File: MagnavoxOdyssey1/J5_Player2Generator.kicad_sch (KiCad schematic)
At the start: 19 parts

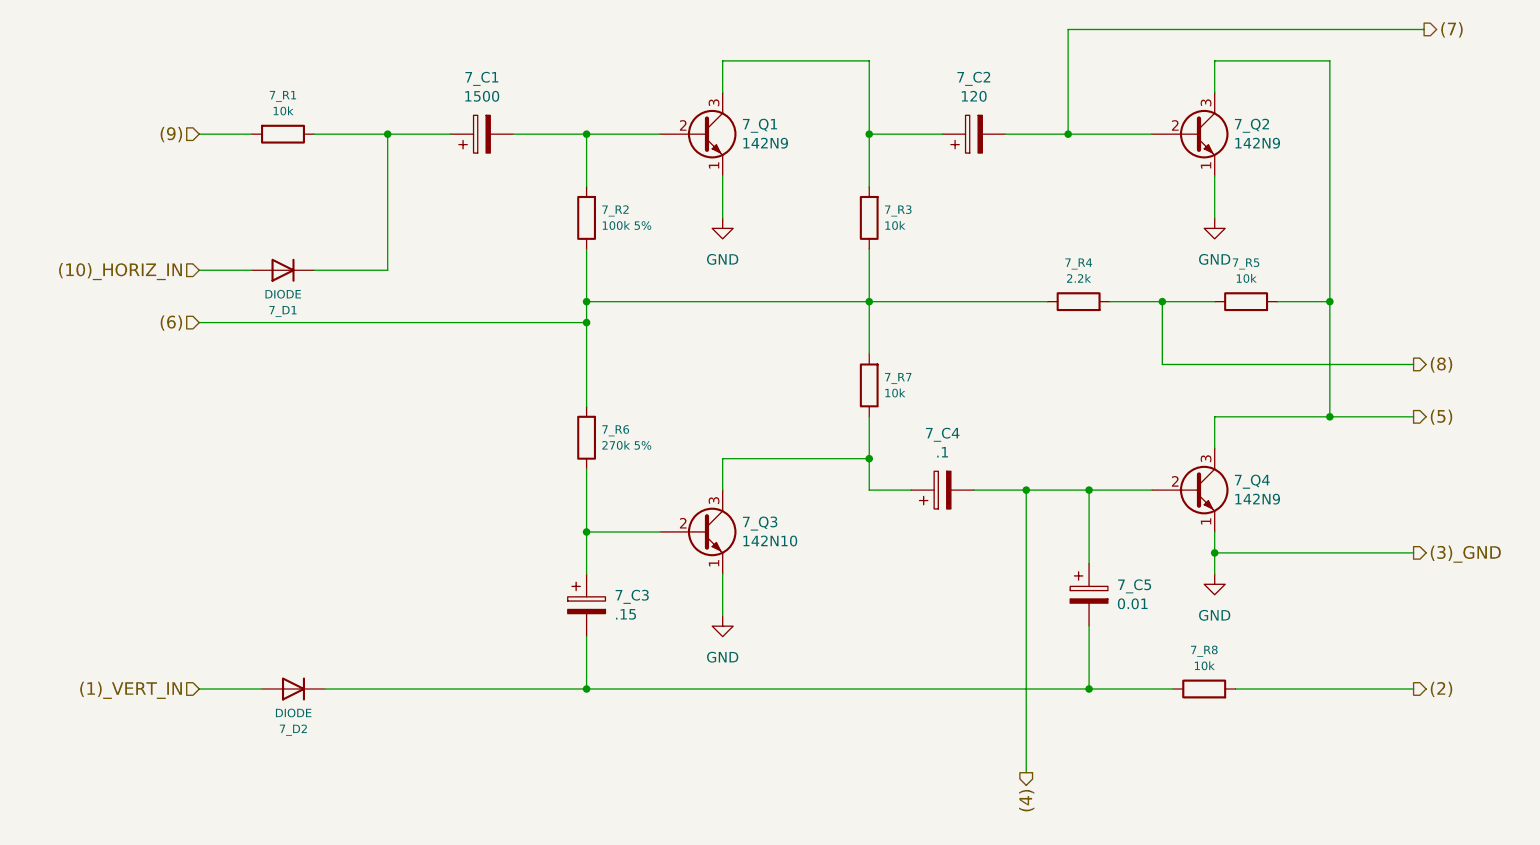
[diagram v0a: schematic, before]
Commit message: update to kicad 9
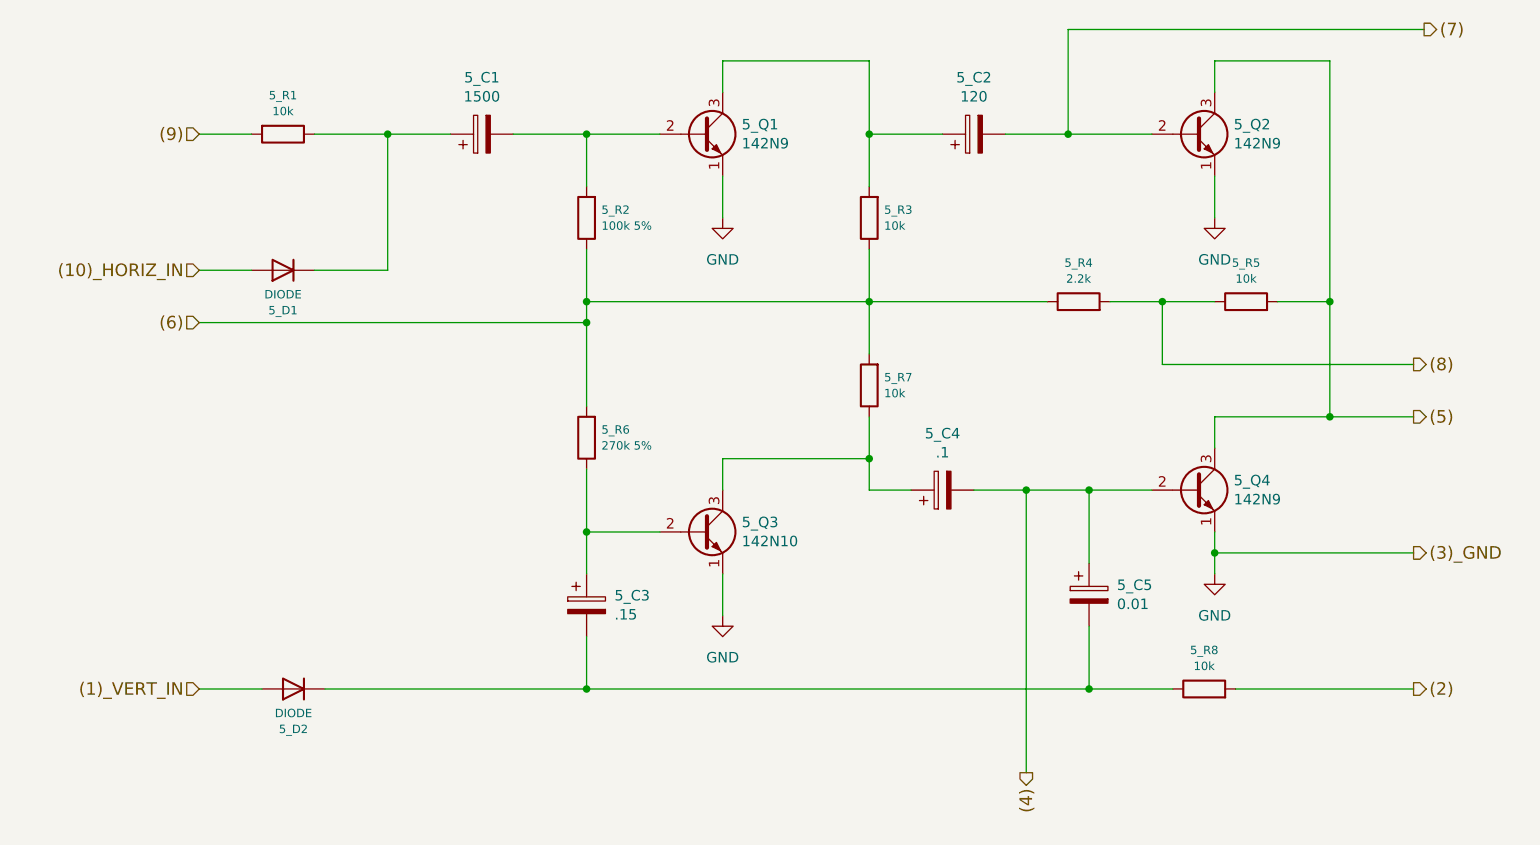
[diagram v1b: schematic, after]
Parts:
- 5_Q1: renamed from 7_Q1; symbol Device:Q_NPN_EBC -> Transistor_BJT:Q_NPN_EBC
- 5_Q2: renamed from 7_Q2; symbol Device:Q_NPN_EBC -> Transistor_BJT:Q_NPN_EBC
- 5_Q3: renamed from 7_Q3; symbol Device:Q_NPN_EBC -> Transistor_BJT:Q_NPN_EBC
- 5_Q4: renamed from 7_Q4; symbol Device:Q_NPN_EBC -> Transistor_BJT:Q_NPN_EBC
- renumbered 7_C1 to 5_C1, 7_C2 to 5_C2, 7_C3 to 5_C3, 7_C4 to 5_C4, 7_C5 to 5_C5, 7_D1 to 5_D1, 7_D2 to 5_D2, 7_R1 to 5_R1, 7_R2 to 5_R2, 7_R3 to 5_R3, 7_R4 to 5_R4, 7_R5 to 5_R5, 7_R6 to 5_R6, 7_R7 to 5_R7, 7_R8 to 5_R8
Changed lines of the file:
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@@
 (kicad_sch
-	(version 20231120)
+	(version 20250114)
 	(generator "eeschema")
-	(generator_version "8.0")
+	(generator_version "9.0")
 	(paper "A4")
 	(junction
@@
 		(on_board yes)
 		(dnp no)
-		(property "Reference" "7_C4"
+		(property "Reference" "5_C4"
 			(at 168.91 99.822 90)
 			(effects
@@
 	)
 	(symbol
-		(lib_id "Device:Q_NPN_EBC")
+		(lib_id "Transistor_BJT:Q_NPN_EBC")
 		(at 139.7 63.5 0)
 		(unit 1)
@@
 		(on_board yes)
 		(dnp no)
-		(property "Reference" "7_Q1"
+		(property "Reference" "5_Q1"
 			(at 144.5514 62.3316 0)
 			(effects
@@
 		(on_board yes)
 		(dnp no)
-		(property "Reference" "7_R2"
+		(property "Reference" "5_R2"
 			(at 127.5334 72.6948 0)
 			(effects
@@
 		(on_board yes)
 		(dnp no)
-		(property "Reference" "7_R5"
+		(property "Reference" "5_R5"
 			(at 205.74 79.121 90)
 			(effects
@@
 		(on_board yes)
 		(dnp no)
-		(property "Reference" "7_R3"
+		(property "Reference" "5_R3"
 			(at 161.8234 72.6948 0)
 			(effects
@@
 	)
 	(symbol
-		(lib_id "Device:Q_NPN_EBC")
+		(lib_id "Transistor_BJT:Q_NPN_EBC")
 		(at 199.39 106.68 0)
 		(unit 1)
@@
 		(on_board yes)
 		(dnp no)
-		(property "Reference" "7_Q4"
+		(property "Reference" "5_Q4"
 			(at 204.2414 105.5116 0)
 			(effects
@@
 	)
 	(symbol
-		(lib_id "Device:Q_NPN_EBC")
+		(lib_id "Transistor_BJT:Q_NPN_EBC")
 		(at 139.7 111.76 0)
 		(unit 1)
@@
 		(on_board yes)
 		(dnp no)
-		(property "Reference" "7_Q3"
+		(property "Reference" "5_Q3"
 			(at 144.5514 110.5916 0)
 			(effects
@@
 		(on_board yes)
 		(dnp no)
-		(property "Reference" "7_R6"
+		(property "Reference" "5_R6"
 			(at 127.5334 99.3648 0)
 			(effects
@@
 		(on_board yes)
 		(dnp no)
-		(property "Reference" "7_R8"
+		(property "Reference" "5_R8"
 			(at 200.66 126.111 90)
 			(effects
@@
 		(on_board yes)
 		(dnp no)
-		(property "Reference" "7_C2"
+		(property "Reference" "5_C2"
 			(at 172.72 56.642 90)
 			(effects
@@
 		(on_board yes)
 		(dnp no)
-		(property "Reference" "7_C3"
+		(property "Reference" "5_C3"
 			(at 129.1082 119.4816 0)
 			(effects
@@
 		(on_board yes)
 		(dnp no)
-		(property "Reference" "7_C5"
+		(property "Reference" "5_C5"
 			(at 190.0682 118.2116 0)
 			(effects
@@
 		(on_board yes)
 		(dnp no)
-		(property "Reference" "7_R4"
+		(property "Reference" "5_R4"
 			(at 185.42 79.121 90)
 			(effects
@@
 		(on_board yes)
 		(dnp no)
-		(property "Reference" "7_C1"
+		(property "Reference" "5_C1"
 			(at 113.03 56.642 90)
 			(effects
@@
 		(on_board yes)
 		(dnp no)
-		(property "Reference" "7_R7"
+		(property "Reference" "5_R7"
 			(at 161.8234 93.0148 0)
 			(effects
@@
 	)
 	(symbol
-		(lib_id "Device:Q_NPN_EBC")
+		(lib_id "Transistor_BJT:Q_NPN_EBC")
 		(at 199.39 63.5 0)
 		(unit 1)
@@
 		(on_board yes)
 		(dnp no)
-		(property "Reference" "7_Q2"
+		(property "Reference" "5_Q2"
 			(at 204.2414 62.3316 0)
 			(effects
@@
 		(on_board yes)
 		(dnp no)
-		(property "Reference" "7_R1"
+		(property "Reference" "5_R1"
 			(at 88.9 58.801 90)
 			(effects
@@
 		(on_board yes)
 		(dnp no)
-		(property "Reference" "7_D2"
+		(property "Reference" "5_D2"
 			(at 90.17 135.6868 0)
 			(effects
@@
 		(on_board yes)
 		(dnp no)
-		(property "Reference" "7_D1"
+		(property "Reference" "5_D1"
 			(at 88.9 84.8868 0)
 			(effects

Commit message: accurate resistors
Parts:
- 5_R2: value 100k 5% -> 100k
- 5_R6: value 270k 5% -> 270k
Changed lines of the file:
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@@
 			)
 		)
-		(property "Value" "100k 5%"
+		(property "Value" "100k"
 			(at 127.5334 74.6252 0)
 			(effects
@@
 			)
 		)
-		(property "Value" "270k 5%"
+		(property "Value" "270k"
 			(at 127.5334 101.2952 0)
 			(effects
